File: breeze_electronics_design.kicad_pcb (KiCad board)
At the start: 2 copper layers, 104.1 x 104.1 mm, 107 parts, among them J1 SIP4, M1 MotorA, M2 MotorB, M3 MotorA, M4 MotorB, Q1 S8050, Q2 SI2302, Q3 SI2302, Q4 SI2302, Q5 SI2302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

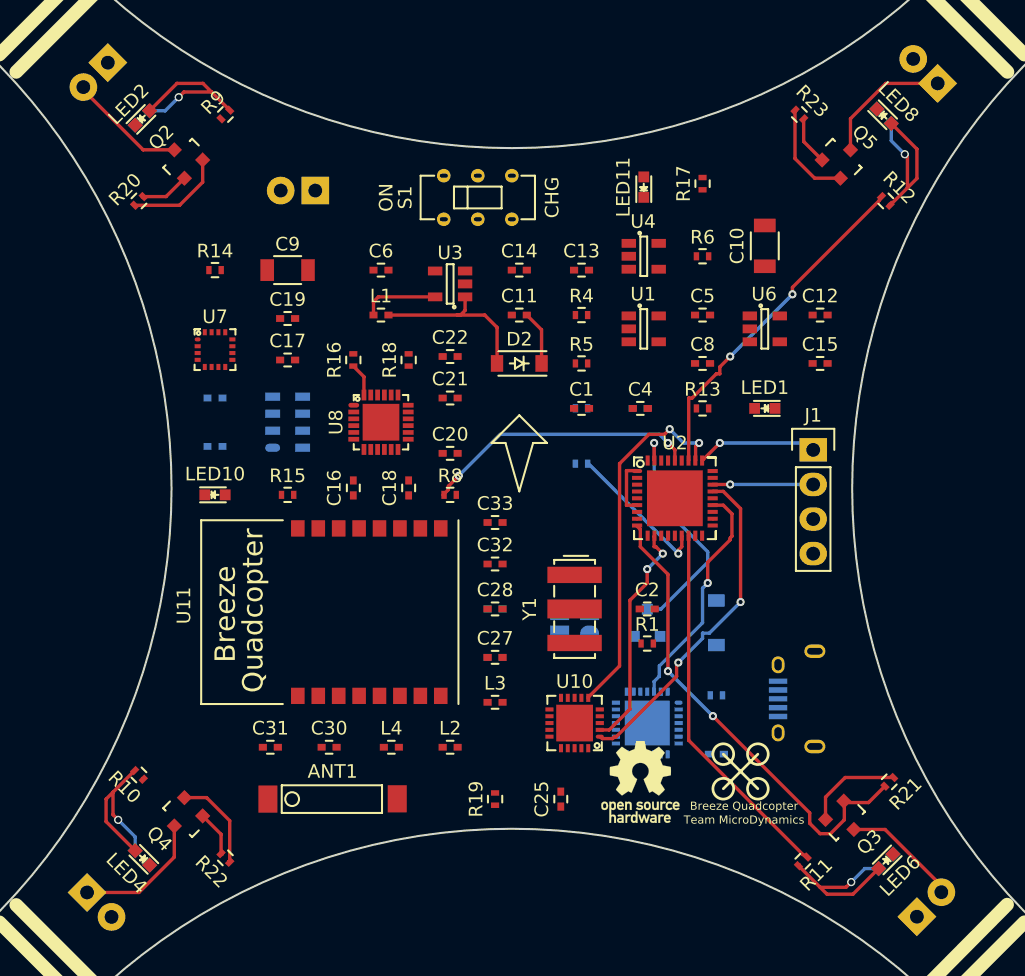
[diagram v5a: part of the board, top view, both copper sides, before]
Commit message: Modify the wiring's layout of Motors
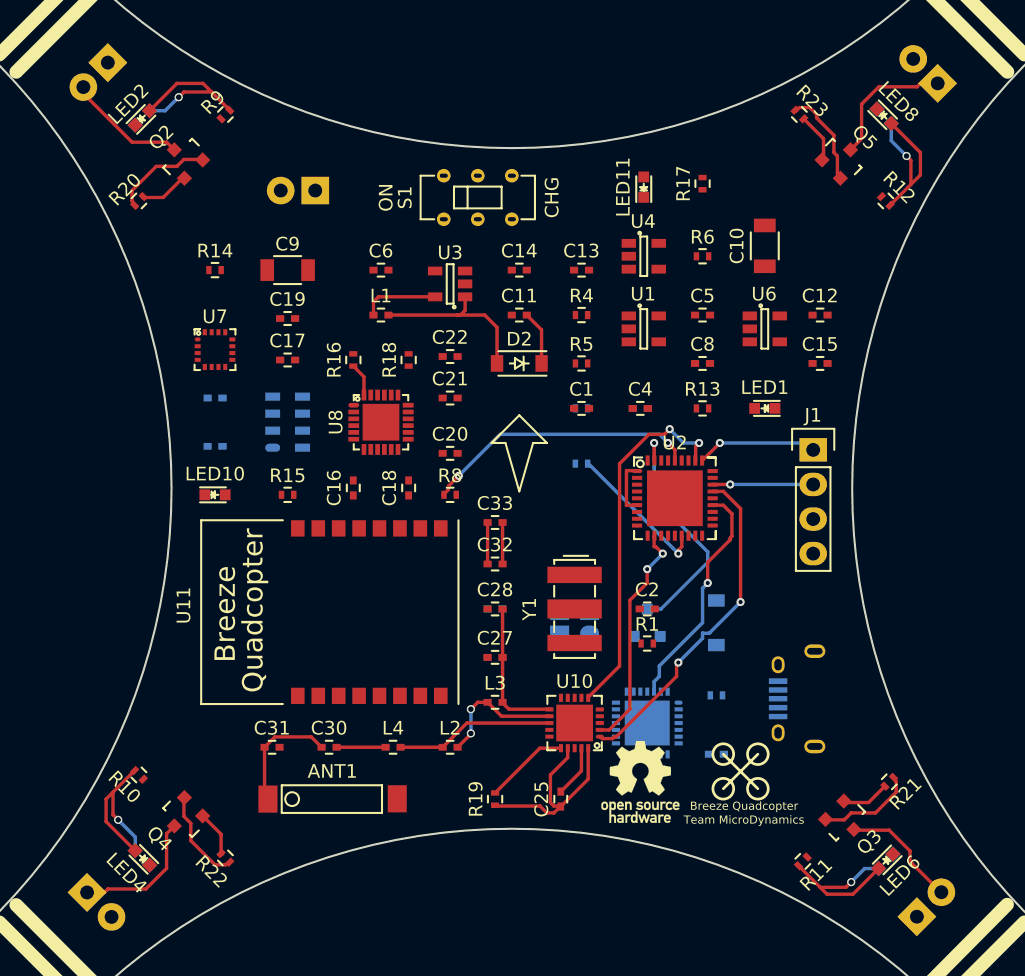
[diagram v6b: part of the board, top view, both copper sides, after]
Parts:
- moved C31 0.13 mm to (128.1, 113.3)
- moved L4 0.13 mm to (137.0, 113.3)
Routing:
- net /PWMC: track 35.4 -> 3.64 mm, vias 2 -> 0
- net /PB1: track 27.3 -> 0.05 mm
- net /PB3: track 25.5 -> 0.02 mm, vias 2 -> 0
- net Net-(C25-Pad1): track 0.00 -> 16.0 mm
- net /ANT2: track 0.00 -> 11.8 mm
- net Net-(C27-Pad1): track 0.00 -> 10.8 mm
- net /ANT1: track 0.00 -> 9.76 mm, vias 0 -> 2
- net Net-(ANT1-Pad1): track 0.00 -> 8.73 mm
- net Net-(R19-Pad2): track 0.00 -> 6.20 mm
- net Net-(C25-Pad2): track 0.00 -> 3.82 mm
- net Net-(C30-Pad1): track 0.00 -> 3.60 mm
- net Net-(C32-Pad2): track 0.00 -> 3.05 mm
- net Net-(C32-Pad1): track 0.00 -> 3.05 mm

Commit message: Modify the layout of footprints accurately
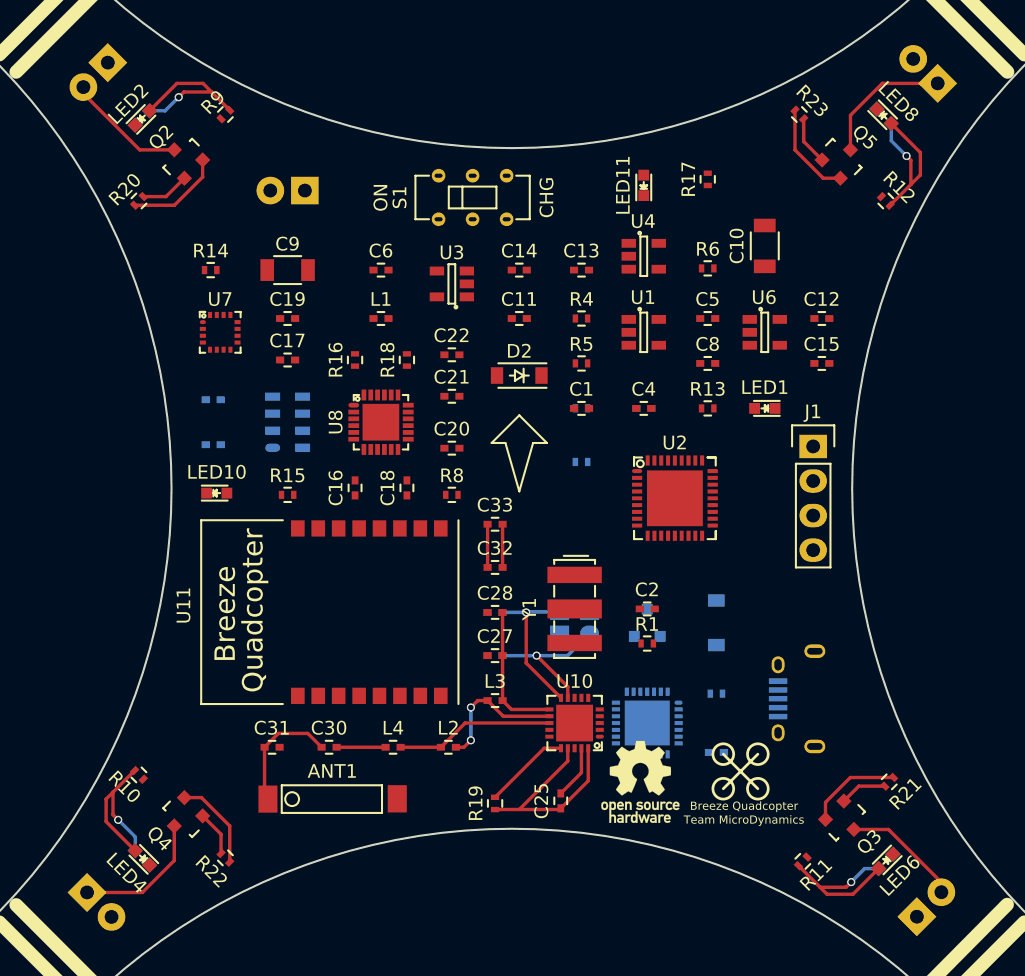
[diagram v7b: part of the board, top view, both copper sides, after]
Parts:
- moved U7 1.33 mm to (124.3, 82.8)
- moved R6 0.97 mm to (160.1, 78.1)
- moved D2 0.89 mm to (146.3, 86.0)
- moved H1 0.76 mm to (130.6, 72.4)
- moved R17 0.50 mm to (160.1, 71.6)
- moved C5 0.46 mm to (160.1, 81.8)
- moved C20 0.40 mm to (141.4, 91.3)
- moved C8 0.38 mm to (160.1, 85.1)
- moved R13 0.38 mm to (160.1, 88.4)
- moved S1 0.38 mm to (142.9, 72.9)
- moved R19 0.32 mm to (144.5, 117.4)
- moved R14 0.32 mm to (123.6, 78.2)
- moved C12 0.28 mm to (168.5, 81.8)
- moved C3 0.25 mm to (155.4, 88.4)
- moved C4 0.25 mm to (155.4, 88.4)
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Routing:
- net /NRF_IRQ: track 26.9 -> 0.00 mm, vias 2 -> 0
- net /CE: track 24.7 -> 0.00 mm, vias 2 -> 0
- net /MP_INT: track 20.3 -> 0.00 mm, vias 2 -> 0
- net /BOOT0: track 17.6 -> 0.00 mm, vias 1 -> 0
- net /RXD_BT: track 17.1 -> 0.02 mm, vias 1 -> 0
- net /CSN: track 16.9 -> 0.00 mm, vias 2 -> 0
- net Net-(D2-Pad2): track 12.7 -> 0.00 mm
- net Net-(C29-Pad2): track 0.00 -> 11.5 mm, vias 0 -> 1
- net Net-(C26-Pad1): track 0.00 -> 11.1 mm, vias 0 -> 1
- net /BAT_DET: track 10.8 -> 0.06 mm, vias 1 -> 0
- net /SWCLK: track 8.90 -> 0.00 mm, vias 1 -> 0
- net /SWDIO: track 7.39 -> 0.00 mm, vias 1 -> 0
- net Net-(C6-Pad1): track 5.65 -> 0.00 mm
- net Net-(U2-Pad1): track 4.12 -> 0.00 mm
- net Net-(C11-Pad1): track 4.01 -> 0.00 mm
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
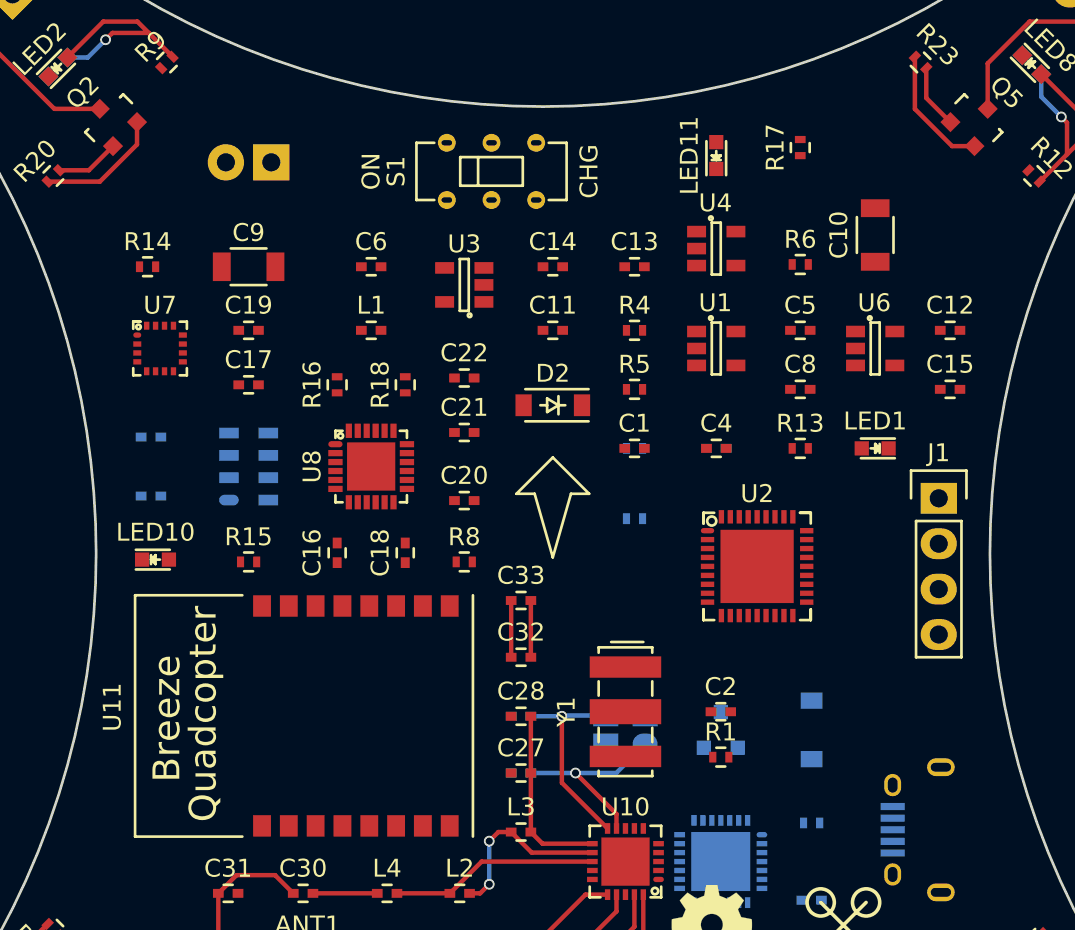
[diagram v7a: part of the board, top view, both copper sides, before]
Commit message: Finish the layout of all footprints
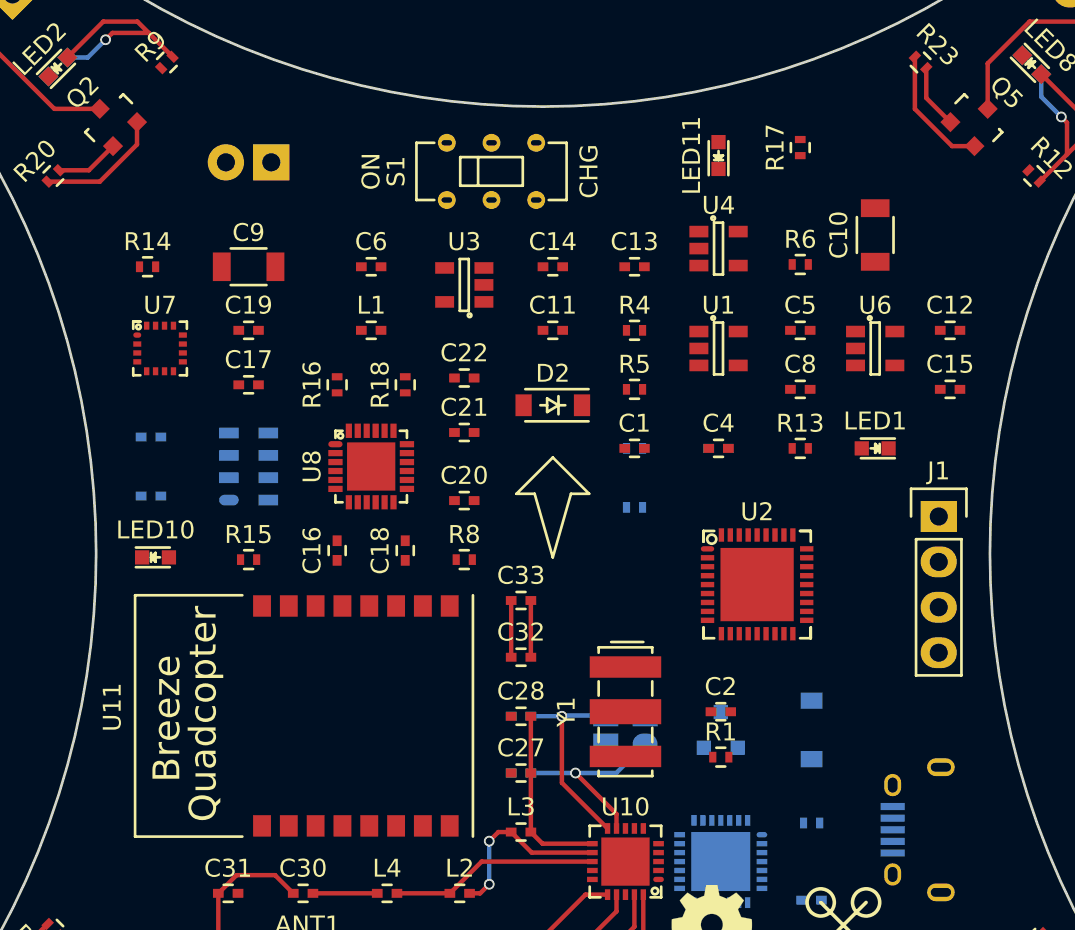
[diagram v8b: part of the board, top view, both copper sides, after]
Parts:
- moved U2 1.02 mm to (157.7, 96.0)
- moved J1 1.02 mm to (167.9, 92.2)
- moved R3 0.63 mm to (150.9, 91.7)
- moved R15 0.13 mm to (129.3, 94.6)
- moved R8 0.13 mm to (141.4, 94.6)
- moved C16 0.13 mm to (134.2, 94.1)
- moved C18 0.13 mm to (138.0, 94.1)
- moved LED10 0.13 mm to (124.1, 94.5)
- moved C3 0.13 mm to (155.6, 88.4)
- moved C4 0.13 mm to (155.6, 88.4)
- moved LED11 0.13 mm to (155.6, 72.0)
- moved U1 0.13 mm to (155.6, 82.8)
- moved U4 0.13 mm to (155.6, 77.2)
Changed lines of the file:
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@@
     (links 163)
     (no_connects 122)
-    (area 75.946 24.638 215.138 163.83)
+    (area 76.182999 24.696999 215.333001 163.847001)
     (thickness 1.6)
     (drawings 20)
-    (tracks 123)
+    (tracks 121)
     (zones 0)
     (modules 107)
@@
   )
   (module Capacitors_SMD:C_0402 (layer B.Cu)
-    (at 155.448 88.392)
+    (at 155.575 88.392)
     (descr "Capacitor SMD 0402, reflow soldering, AVX (see smccp.pdf)")
     (tags "capacitor 0402")
@@
   )
   (module Capacitors_SMD:C_0402 (layer F.Cu)
-    (at 155.448 88.392)
+    (at 155.575 88.392)
     (descr "Capacitor SMD 0402, reflow soldering, AVX (see smccp.pdf)")
     (tags "capacitor 0402")
@@
   )
   (module Capacitors_SMD:C_0402 (layer F.Cu)
-    (at 134.239 94.234 270)
+    (at 134.239 94.107 270)
     (descr "Capacitor SMD 0402, reflow soldering, AVX (see smccp.pdf)")
     (tags "capacitor 0402")
@@
   )
   (module Capacitors_SMD:C_0402 (layer F.Cu)
-    (at 138.049 94.234 90)
+    (at 138.049 94.107 90)
     (descr "Capacitor SMD 0402, reflow soldering, AVX (see smccp.pdf)")
     (tags "capacitor 0402")
@@
   )
   (module Pin_Headers:Pin_Header_Straight_1x04 (layer F.Cu)
-    (at 167.894 91.186)
+    (at 167.894 92.202)
     (descr "Through hole pin header")
     (tags "pin header")
@@
   )
   (module LEDs:LED_0603 (layer F.Cu)
-    (at 124.079 94.615)
+    (at 124.079 94.488)
     (descr "LED 0603 smd package")
     (tags "LED led 0603 SMD smd SMT smt smdled SMDLED smtled SMTLED")
@@
   )
   (module LEDs:LED_0603 (layer F.Cu)
-    (at 155.448 72.009 90)
+    (at 155.575 72.009 90)
     (descr "LED 0603 smd package")
     (tags "LED led 0603 SMD smd SMT smt smdled SMDLED smtled SMTLED")
@@
   )
   (module Resistors_SMD:R_0402 (layer B.Cu)
-    (at 150.876 92.329 180)
+    (at 150.876 91.694 180)
     (descr "Resistor SMD 0402, reflow soldering, Vishay (see dcrcw.pdf)")
     (tags "resistor 0402")
@@
   )
   (module Resistors_SMD:R_0402 (layer F.Cu)
-    (at 141.351 94.742)
+    (at 141.351 94.615)
     (descr "Resistor SMD 0402, reflow soldering, Vishay (see dcrcw.pdf)")
     (tags "resistor 0402")
@@
   )
   (module Resistors_SMD:R_0402 (layer F.Cu)
-    (at 129.286 94.742 180)
+    (at 129.286 94.615 180)
     (descr "Resistor SMD 0402, reflow soldering, Vishay (see dcrcw.pdf)")
     (tags "resistor 0402")
@@
   )
   (module TO_SOT_Packages_SMD:SOT-23-5 (layer F.Cu)
-    (at 155.448 82.804)
+    (at 155.575 82.804)
     (descr "5-pin SOT23 package")
     (tags SOT-23-5)
     (attr smd)
-    (fp_text reference U1 (at -0.05 -2.55) (layer F.SilkS)
+    (fp_text reference U1 (at 0 -2.413) (layer F.SilkS)
       (effects (font (size 1 1) (thickness 0.15)))
     )
@@
   )
   (module Footprint:VFQFPN_STM32F103T8U6TR (layer F.Cu)
-    (at 157.734 94.996)
+    (at 157.734 96.012)
     (descr "MCU STM32F103T8U6TR")
     (tags "MCU STM32F103T8U6TR")
@@
     (tags SOT-23-5)
     (attr smd)
-    (fp_text reference U3 (at 0 2.286 180) (layer F.SilkS)
+    (fp_text reference U3 (at 0 2.413 180) (layer F.SilkS)
       (effects (font (size 1 1) (thickness 0.15)))
     )
@@
   )
   (module TO_SOT_Packages_SMD:SOT-23-5 (layer F.Cu)
-    (at 155.448 77.216)
+    (at 155.575 77.216)
     (descr "5-pin SOT23 package")
     (tags SOT-23-5)
     (attr smd)
-    (fp_text reference U4 (at -0.05 -2.55) (layer F.SilkS)
+    (fp_text reference U4 (at 0 -2.413) (layer F.SilkS)
       (effects (font (size 1 1) (thickness 0.15)))
     )
@@
     (tags SOT-23-5)
     (attr smd)
-    (fp_text reference U6 (at -0.05 -2.55) (layer F.SilkS)
+    (fp_text reference U6 (at 0 -2.413) (layer F.SilkS)
       (effects (font (size 1 1) (thickness 0.15)))
     )
@@
   (segment (start 127.593 113.284) (end 127.593 116.8488) (width 0.25) (layer F.Cu) (net 1))
   (segment (start 127.593 116.8488) (end 127.8382 117.094) (width 0.25) (layer F.Cu) (net 1))
-  (segment (start 151.384 92.456) (end 151.326 92.456) (width 0.25) (layer B.Cu) (net 6) (status 80000))
   (segment (start 149.868 113.356) (end 149.868 114.292) (width 0.25) (layer F.Cu) (net 35))
   (segment (start 149.868 114.292) (end 146.304 117.856) (width 0.25) (layer F.Cu) (net 35))
@@
   (segment (start 168.638396 71.483396) (end 169.890107 71.483396) (width 0.25) (layer F.Cu) (net 87))
   (segment (start 166.559802 69.404802) (end 168.638396 71.483396) (width 0.25) (layer F.Cu) (net 87))
-  (segment (start 149.368 113.356) (end 148.1315 113.356) (width 0.25) (layer F.Cu) (net 107) (status 400000))
-  (segment (start 148.1315 113.356) (end 144.526 116.9615) (width 0.25) (layer F.Cu) (net 107) (status 800000))
-  (segment (start 156.21 109.22) (end 156.202 109.206) (width 0.25) (layer B.Cu) (net 119) (status 80000))
+  (segment (start 149.368 113.356) (end 148.1315 113.356) (width 0.25) (layer F.Cu) (net 107))
+  (segment (start 148.1315 113.356) (end 144.526 116.9615) (width 0.25) (layer F.Cu) (net 107))
 )
